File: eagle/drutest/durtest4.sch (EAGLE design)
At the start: 80 parts, among them IC1 XCF02S, IC2 25LC080SN, Q5 BC848SMD, Q6 BC848SMD, Q7 BC848SMD, Q8 BC848SMD, T1 BSS138, T2 BC848, T3 BSS138, U1 XC3S400TQ144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

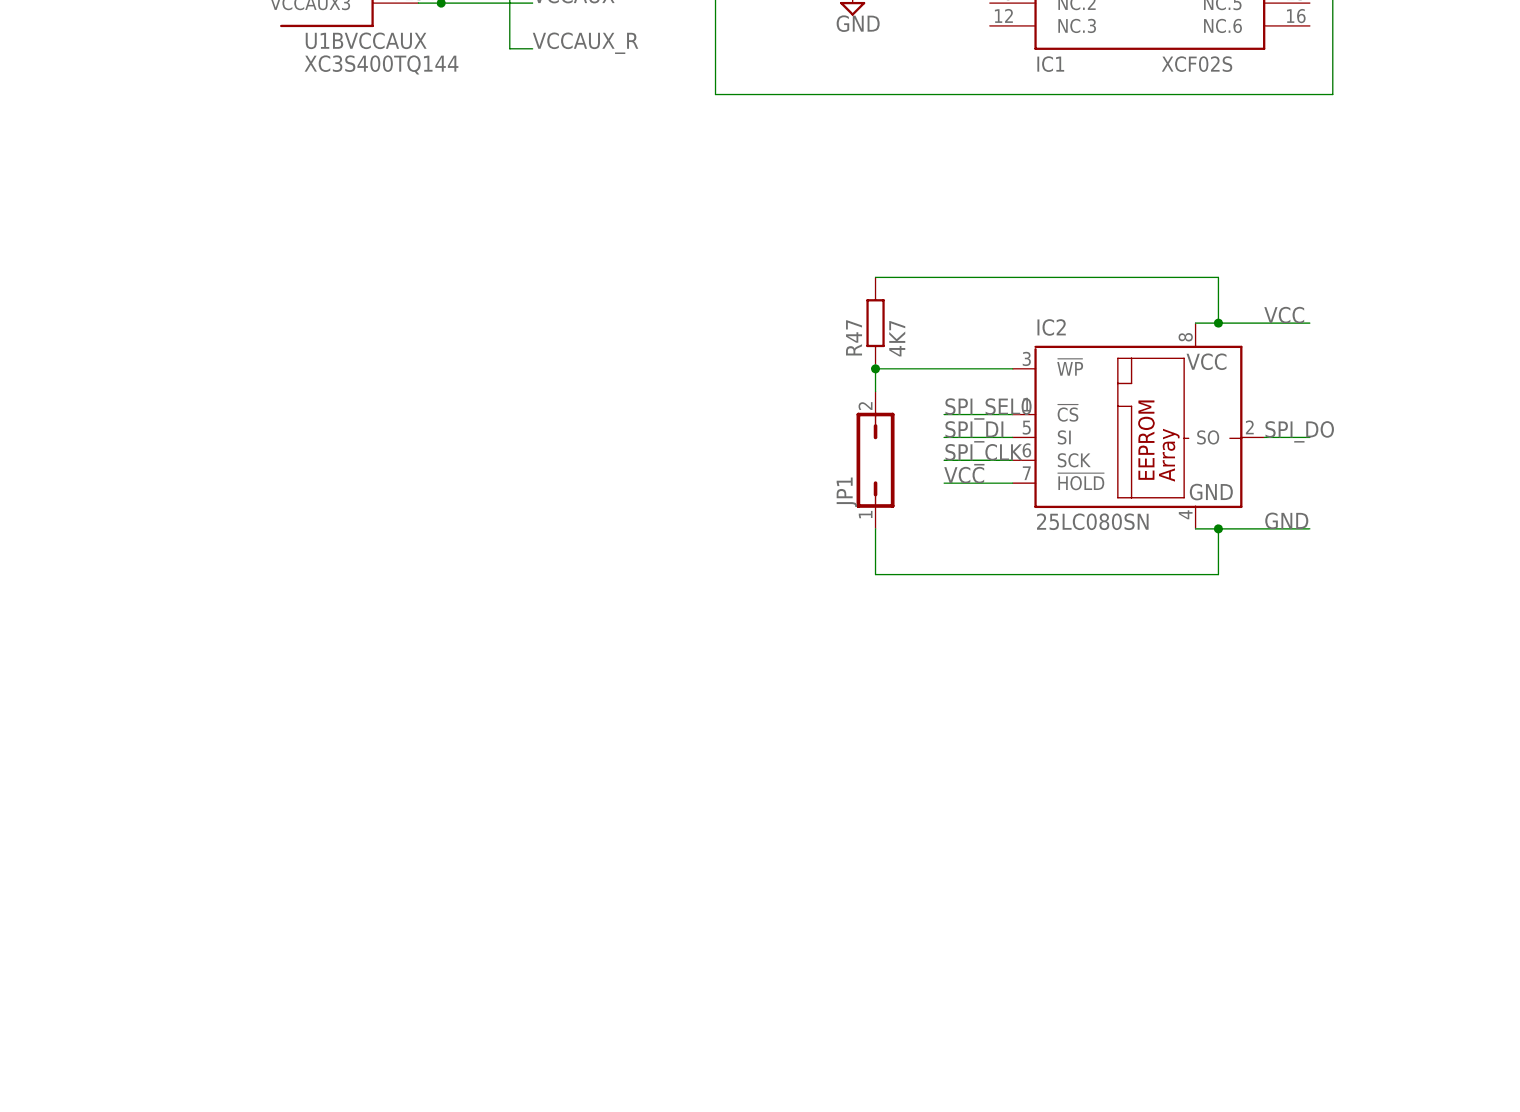
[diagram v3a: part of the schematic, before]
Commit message: added bare atmega chip
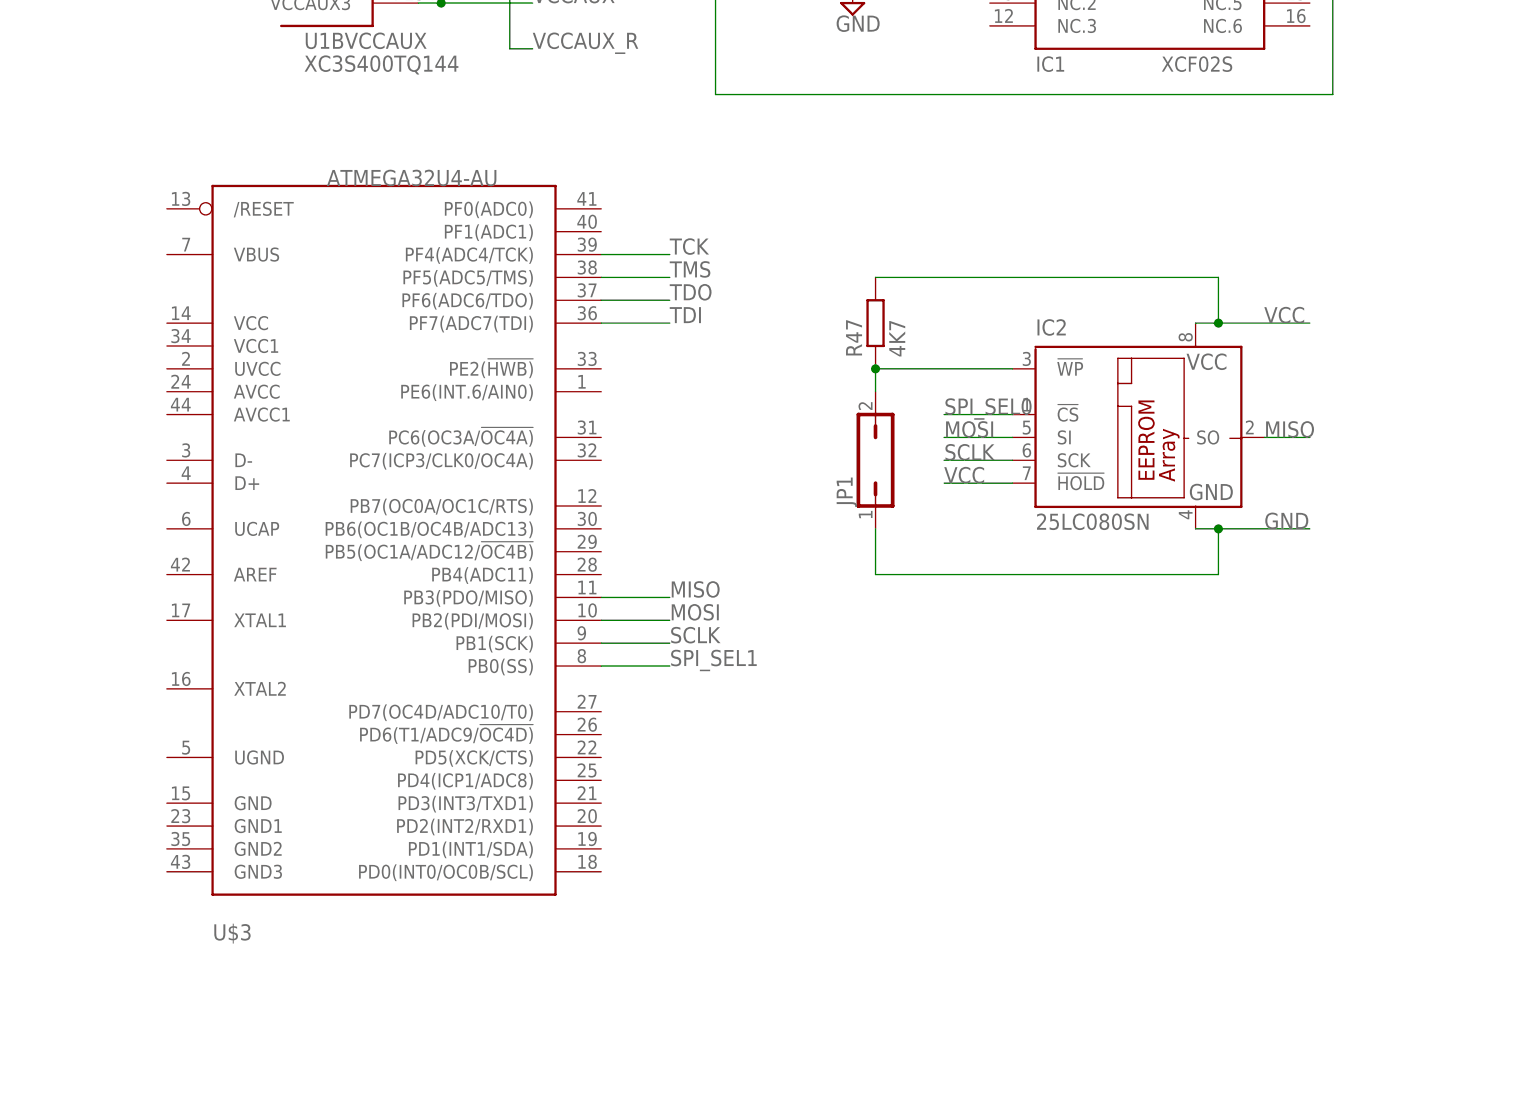
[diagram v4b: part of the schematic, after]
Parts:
- added U$3: ATMEGA32U4-AU, adafruit:ATMEGA32U4-AU
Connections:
- removed net SPI_CLK: IC2.SCK
- removed net SPI_DI: IC2.SI
- removed net SPI_DO: IC2.SO
- new net MISO: IC2.SO, U$3.PB3(PDO/MISO)
- new net MOSI: IC2.SI, U$3.PB2(PDI/MOSI)
- new net SCLK: IC2.SCK, U$3.PB1(SCK)
- new net SPI_SEL1: U$3.PB0(SS)
- net TCK: now also U$3.PF4(ADC4/TCK)
- net TDI: now also U$3.PF7(ADC7(TDI)
- net TDO: now also U$3.PF6(ADC6/TDO)
- net TMS: now also U$3.PF5(ADC5/TMS)
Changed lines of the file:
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@@
 <layer number="53" name="tGND_GNDA" color="7" fill="9" visible="no" active="no"/>
 <layer number="54" name="bGND_GNDA" color="1" fill="9" visible="no" active="no"/>
+<layer number="56" name="wert" color="7" fill="1" visible="no" active="no"/>
 <layer number="91" name="Nets" color="2" fill="1" visible="yes" active="yes"/>
 <layer number="92" name="Busses" color="1" fill="1" visible="yes" active="yes"/>
@@
 <layer number="97" name="Info" color="7" fill="1" visible="yes" active="yes"/>
 <layer number="98" name="Guide" color="6" fill="1" visible="yes" active="yes"/>
+<layer number="100" name="Muster" color="7" fill="1" visible="no" active="no"/>
+<layer number="101" name="Patch_Top" color="12" fill="4" visible="yes" active="yes"/>
+<layer number="102" name="Vscore" color="7" fill="1" visible="yes" active="yes"/>
+<layer number="103" name="fp3" color="7" fill="1" visible="no" active="yes"/>
+<layer number="104" name="Name" color="7" fill="1" visible="yes" active="yes"/>
+<layer number="105" name="Beschreib" color="9" fill="1" visible="yes" active="yes"/>
+<layer number="106" name="BGA-Top" color="4" fill="1" visible="yes" active="yes"/>
+<layer number="107" name="BD-Top" color="5" fill="1" visible="yes" active="yes"/>
+<layer number="108" name="fp8" color="7" fill="1" visible="no" active="yes"/>
+<layer number="109" name="fp9" color="7" fill="1" visible="no" active="yes"/>
+<layer number="110" name="fp0" color="7" fill="1" visible="no" active="yes"/>
+<layer number="111" name="LPC17xx" color="7" fill="1" visible="yes" active="yes"/>
+<layer number="112" name="tSilk" color="7" fill="1" visible="yes" active="yes"/>
+<layer number="116" name="Patch_BOT" color="9" fill="4" visible="yes" active="yes"/>
+<layer number="121" name="_tsilk" color="7" fill="1" visible="yes" active="yes"/>
+<layer number="122" name="_bsilk" color="7" fill="1" visible="yes" active="yes"/>
+<layer number="123" name="tTestmark" color="7" fill="1" visible="no" active="yes"/>
+<layer number="124" name="bTestmark" color="7" fill="1" visible="no" active="yes"/>
+<layer number="125" name="_tNames" color="7" fill="1" visible="yes" active="yes"/>
+<layer number="126" name="_bNames" color="7" fill="1" visible="yes" active="yes"/>
+<layer number="127" name="_tValues" color="7" fill="1" visible="yes" active="yes"/>
+<layer number="128" name="_bValues" color="7" fill="1" visible="yes" active="yes"/>
+<layer number="131" name="tAdjust" color="7" fill="1" visible="no" active="yes"/>
+<layer number="132" name="bAdjust" color="7" fill="1" visible="no" active="yes"/>
+<layer number="144" name="Drill_legend" color="7" fill="1" visible="yes" active="yes"/>
+<layer number="151" name="HeatSink" color="7" fill="1" visible="yes" active="yes"/>
+<layer number="152" name="_bDocu" color="7" fill="1" visible="yes" active="yes"/>
+<layer number="199" name="Contour" color="7" fill="1" visible="yes" active="yes"/>
+<layer number="200" name="200bmp" color="1" fill="10" visible="yes" active="yes"/>
+<layer number="201" name="201bmp" color="2" fill="1" visible="no" active="no"/>
+<layer number="202" name="202bmp" color="3" fill="1" visible="no" active="no"/>
+<layer number="203" name="203bmp" color="4" fill="10" visible="yes" active="yes"/>
+<layer number="204" name="204bmp" color="5" fill="10" visible="yes" active="yes"/>
+<layer number="205" name="205bmp" color="6" fill="10" visible="yes" active="yes"/>
+<layer number="206" name="206bmp" color="7" fill="10" visible="yes" active="yes"/>
+<layer number="207" name="207bmp" color="8" fill="10" visible="yes" active="yes"/>
+<layer number="208" name="208bmp" color="9" fill="10" visible="yes" active="yes"/>
+<layer number="209" name="209bmp" color="7" fill="1" visible="no" active="yes"/>
+<layer number="210" name="210bmp" color="7" fill="1" visible="no" active="yes"/>
+<layer number="211" name="211bmp" color="7" fill="1" visible="yes" active="yes"/>
+<layer number="212" name="212bmp" color="7" fill="1" visible="yes" active="yes"/>
+<layer number="213" name="213bmp" color="7" fill="1" visible="yes" active="yes"/>
+<layer number="214" name="214bmp" color="7" fill="1" visible="yes" active="yes"/>
+<layer number="215" name="215bmp" color="7" fill="1" visible="yes" active="yes"/>
+<layer number="216" name="216bmp" color="7" fill="1" visible="yes" active="yes"/>
+<layer number="217" name="217bmp" color="18" fill="1" visible="no" active="no"/>
+<layer number="218" name="218bmp" color="19" fill="1" visible="no" active="no"/>
+<layer number="219" name="219bmp" color="20" fill="1" visible="no" active="no"/>
+<layer number="220" name="220bmp" color="21" fill="1" visible="no" active="no"/>
+<layer number="221" name="221bmp" color="22" fill="1" visible="no" active="no"/>
+<layer number="222" name="222bmp" color="23" fill="1" visible="no" active="no"/>
+<layer number="223" name="223bmp" color="24" fill="1" visible="no" active="no"/>
+<layer number="224" name="224bmp" color="25" fill="1" visible="no" active="no"/>
+<layer number="248" name="Housing" color="7" fill="1" visible="yes" active="yes"/>
+<layer number="249" name="Edge" color="7" fill="1" visible="yes" active="yes"/>
 <layer number="250" name="Descript" color="3" fill="1" visible="no" active="no"/>
 <layer number="251" name="SMDround" color="4" fill="9" visible="no" active="yes"/>
+<layer number="254" name="cooling" color="7" fill="1" visible="yes" active="yes"/>
 </layers>
 <schematic xreflabel="%F%N/%S.%C%R" xrefpart="/%S.%C%R">
@@
 <part name="RESET_SW" library="jumper" deviceset="JP1Q" device=""/>
 <part name="R52" library="resistor" deviceset="R-EU_" device="M0805" value="4K7"/>
+<part name="U$3" library="adafruit" deviceset="ATMEGA32U4" device="-AU"/>
 </parts>
 <sheets>
@@
 <instance part="RESET_SW" gate="A" x="81.28" y="-76.2" rot="R90"/>
 <instance part="R52" gate="G$1" x="81.28" y="-83.82"/>
+<instance part="U$3" gate="G$1" x="-160.02" y="-139.7"/>
 </instances>
 <busses>
@@
 <label x="-73.66" y="-15.24" size="1.778" layer="95"/>
 </segment>
+<segment>
+<pinref part="U$3" gate="G$1" pin="PF4(ADC4/TCK)"/>
+<wire x1="-127" y1="-101.6" x2="-134.62" y2="-101.6" width="0.1524" layer="91"/>
+<label x="-127" y="-101.6" size="1.778" layer="95"/>
+</segment>
 </net>
 <net name="TMS" class="0">
@@
 <label x="-73.66" y="-12.7" size="1.778" layer="95"/>
 </segment>
+<segment>
+<pinref part="U$3" gate="G$1" pin="PF5(ADC5/TMS)"/>
+<wire x1="-127" y1="-104.14" x2="-134.62" y2="-104.14" width="0.1524" layer="91"/>
+<label x="-127" y="-104.14" size="1.778" layer="95"/>
+</segment>
 </net>
 <net name="TDI" class="0">
@@
 <label x="-83.82" y="-20.32" size="1.778" layer="95"/>
 </segment>
+<segment>
+<pinref part="U$3" gate="G$1" pin="PF7(ADC7(TDI)"/>
+<wire x1="-127" y1="-109.22" x2="-134.62" y2="-109.22" width="0.1524" layer="91"/>
+<label x="-127" y="-109.22" size="1.778" layer="95"/>
+</segment>
 </net>
 <net name="TDO" class="0">
@@
 <wire x1="-83.82" y1="-15.24" x2="-104.14" y2="-15.24" width="0.1524" layer="91"/>
 <label x="-83.82" y="-15.24" size="1.778" layer="95"/>
+</segment>
+<segment>
+<pinref part="U$3" gate="G$1" pin="PF6(ADC6/TDO)"/>
+<wire x1="-127" y1="-106.68" x2="-134.62" y2="-106.68" width="0.1524" layer="91"/>
+<label x="-127" y="-106.68" size="1.778" layer="95"/>
 </segment>
 </net>
@@
 </segment>
 </net>
-<net name="SPI_CLK" class="0">
+<net name="SCLK" class="0">
 <segment>
 <pinref part="IC2" gate="G$1" pin="SCK"/>
@@
 <label x="-96.52" y="-124.46" size="1.778" layer="95"/>
 </segment>
-</net>
-<net name="SPI_DI" class="0">
+<segment>
+<pinref part="U$3" gate="G$1" pin="PB1(SCK)"/>
+<wire x1="-127" y1="-144.78" x2="-134.62" y2="-144.78" width="0.1524" layer="91"/>
+<label x="-127" y="-144.78" size="1.778" layer="95"/>
+</segment>
+</net>
+<net name="MOSI" class="0">
 <segment>
 <pinref part="IC2" gate="G$1" pin="SI"/>
@@
 <label x="-96.52" y="-121.92" size="1.778" layer="95"/>
 </segment>
-</net>
-<net name="SPI_DO" class="0">
+<segment>
+<pinref part="U$3" gate="G$1" pin="PB2(PDI/MOSI)"/>
+<wire x1="-127" y1="-142.24" x2="-134.62" y2="-142.24" width="0.1524" layer="91"/>
+<label x="-127" y="-142.24" size="1.778" layer="95"/>
+</segment>
+</net>
+<net name="MISO" class="0">
 <segment>
 <pinref part="IC2" gate="G$1" pin="SO"/>
 <wire x1="-55.88" y1="-121.92" x2="-60.96" y2="-121.92" width="0.1524" layer="91"/>
 <label x="-60.96" y="-121.92" size="1.778" layer="95"/>
+</segment>
+<segment>
+<pinref part="U$3" gate="G$1" pin="PB3(PDO/MISO)"/>
+<wire x1="-127" y1="-139.7" x2="-134.62" y2="-139.7" width="0.1524" layer="91"/>
+<label x="-127" y="-139.7" size="1.778" layer="95"/>
 </segment>
 </net>
@@
 </segment>
 </net>
+<net name="SPI_SEL1" class="0">
+<segment>
+<pinref part="U$3" gate="G$1" pin="PB0(SS)"/>
+<wire x1="-127" y1="-147.32" x2="-134.62" y2="-147.32" width="0.1524" layer="91"/>
+<label x="-127" y="-147.32" size="1.778" layer="95"/>
+</segment>
+</net>
